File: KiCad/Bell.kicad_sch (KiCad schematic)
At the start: 29 parts, among them J1 USB-C, J2 POWER, J3 Conn_01x10, U1 ESP32-WROOM-32, U2 FT231XQ, U3 ISL89410, U4 ISL89410, U5 LMR16006YQ3, U6 AA, U7 QR

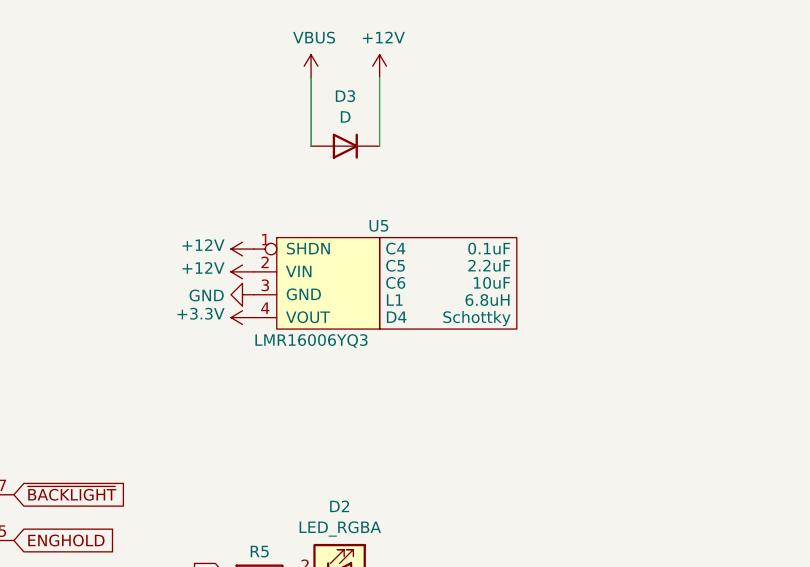
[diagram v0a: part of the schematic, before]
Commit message: More KiCad 6 tweaks
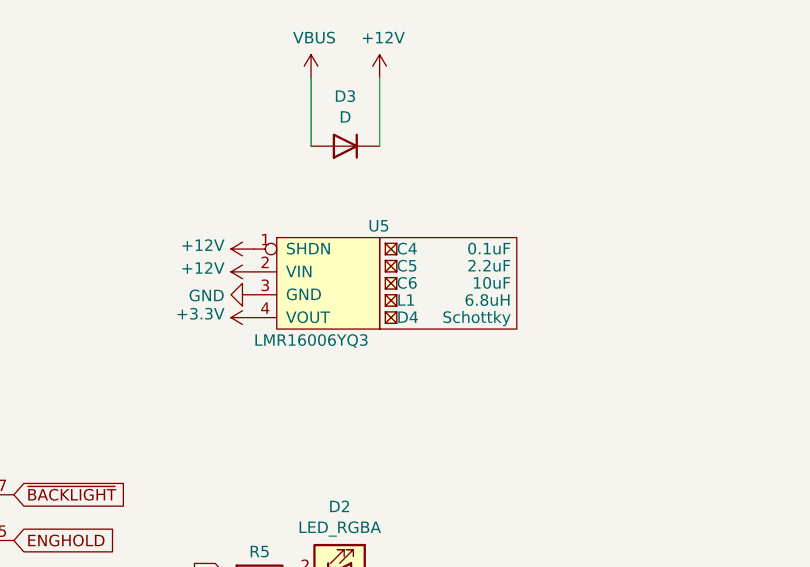
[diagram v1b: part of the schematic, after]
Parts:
- U1: footprint RevK:ESP32-WROOM-32 -> RF_Module:ESP32-WROOM-32
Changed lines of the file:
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@@
   (title_block
     (title "bell box control")
-    (date "2021-07-20")
+    (date "${DATE}")
     (rev "2")
     (company "Adrian Kennard Andrews & Arnold Ltd")
@@
     (property "Reference" "U1" (id 0) (at 53.34 23.3426 0))
     (property "Value" "ESP32-WROOM-32" (id 1) (at 53.34 25.654 0))
-    (property "Footprint" "RevK:ESP32-WROOM-32" (id 2) (at 53.34 101.6 0)
+    (property "Footprint" "RF_Module:ESP32-WROOM-32" (id 2) (at 53.34 101.6 0)
       (effects (font (size 1.27 1.27)) hide)
     )
@@
     (pin "4")
   )
-  (symbol (lib_id "RevK:Hidden") (at 206.375 58.42 0) (unit 1)
-    (in_bom yes) (on_board yes)
-    (property "Reference" "C4" (id 0) (at 205.74 58.42 0)
+  (symbol (lib_name "Hidden_2") (lib_id "RevK:Hidden") (at 206.375 58.42 0) (unit 1)
+    (in_bom yes) (on_board yes)
+    (property "Reference" "C4" (id 0) (at 207.01 58.42 0)
       (effects (font (size 1.27 1.27)) (justify left))
     )
@@
       (effects (font (size 1.27 1.27)) hide)
     )
+    (property "Part No" "" (id 5) (at 206.375 58.42 0)
+      (effects (font (size 1.27 1.27)) hide)
+    )
     (pin "~")
   )
-  (symbol (lib_id "RevK:Hidden") (at 206.375 60.325 0) (unit 1)
-    (in_bom yes) (on_board yes)
-    (property "Reference" "C5" (id 0) (at 205.74 60.325 0)
+  (symbol (lib_name "Hidden_4") (lib_id "RevK:Hidden") (at 206.375 60.325 0) (unit 1)
+    (in_bom yes) (on_board yes)
+    (property "Reference" "C5" (id 0) (at 207.01 60.325 0)
       (effects (font (size 1.27 1.27)) (justify left))
     )
@@
       (effects (font (size 1.27 1.27)) hide)
     )
+    (property "Part No" "" (id 5) (at 206.375 60.325 0)
+      (effects (font (size 1.27 1.27)) hide)
+    )
     (pin "~")
   )
-  (symbol (lib_id "RevK:Hidden") (at 206.375 62.23 0) (unit 1)
-    (in_bom yes) (on_board yes)
-    (property "Reference" "C6" (id 0) (at 205.74 62.23 0)
+  (symbol (lib_name "Hidden_3") (lib_id "RevK:Hidden") (at 206.375 62.23 0) (unit 1)
+    (in_bom yes) (on_board yes)
+    (property "Reference" "C6" (id 0) (at 207.01 62.23 0)
       (effects (font (size 1.27 1.27)) (justify left))
     )
@@
       (effects (font (size 1.27 1.27)) hide)
     )
+    (property "Part No" "" (id 5) (at 206.375 62.23 0)
+      (effects (font (size 1.27 1.27)) hide)
+    )
     (pin "~")
   )
-  (symbol (lib_id "RevK:Hidden") (at 206.375 64.135 0) (unit 1)
-    (in_bom yes) (on_board yes)
-    (property "Reference" "L1" (id 0) (at 205.74 64.135 0)
+  (symbol (lib_name "Hidden_1") (lib_id "RevK:Hidden") (at 206.375 64.135 0) (unit 1)
+    (in_bom yes) (on_board yes)
+    (property "Reference" "L1" (id 0) (at 207.01 64.135 0)
       (effects (font (size 1.27 1.27)) (justify left))
     )
@@
       (effects (font (size 1.27 1.27)) hide)
     )
+    (property "Note" "" (id 6) (at 206.375 64.135 0)
+      (effects (font (size 1.27 1.27)) hide)
+    )
     (pin "~")
   )
   (symbol (lib_id "RevK:Hidden") (at 206.375 66.04 0) (unit 1)
     (in_bom yes) (on_board yes)
-    (property "Reference" "D4" (id 0) (at 205.74 66.04 0)
+    (property "Reference" "D4" (id 0) (at 207.01 66.04 0)
       (effects (font (size 1.27 1.27)) (justify left))
     )
@@
     )
     (property "Part No" "CD1206-B2100" (id 5) (at 206.375 66.04 0)
+      (effects (font (size 1.27 1.27)) hide)
+    )
+    (property "Note" "" (id 6) (at 206.375 66.04 0)
       (effects (font (size 1.27 1.27)) hide)
     )
@@
     )
     (path "/00000000-0000-0000-0000-00006043326c"
-      (reference "U1") (unit 1) (value "ESP32-WROOM-32") (footprint "RevK:ESP32-WROOM-32")
+      (reference "U1") (unit 1) (value "ESP32-WROOM-32") (footprint "RF_Module:ESP32-WROOM-32")
     )
     (path "/00000000-0000-0000-0000-00006084108b"

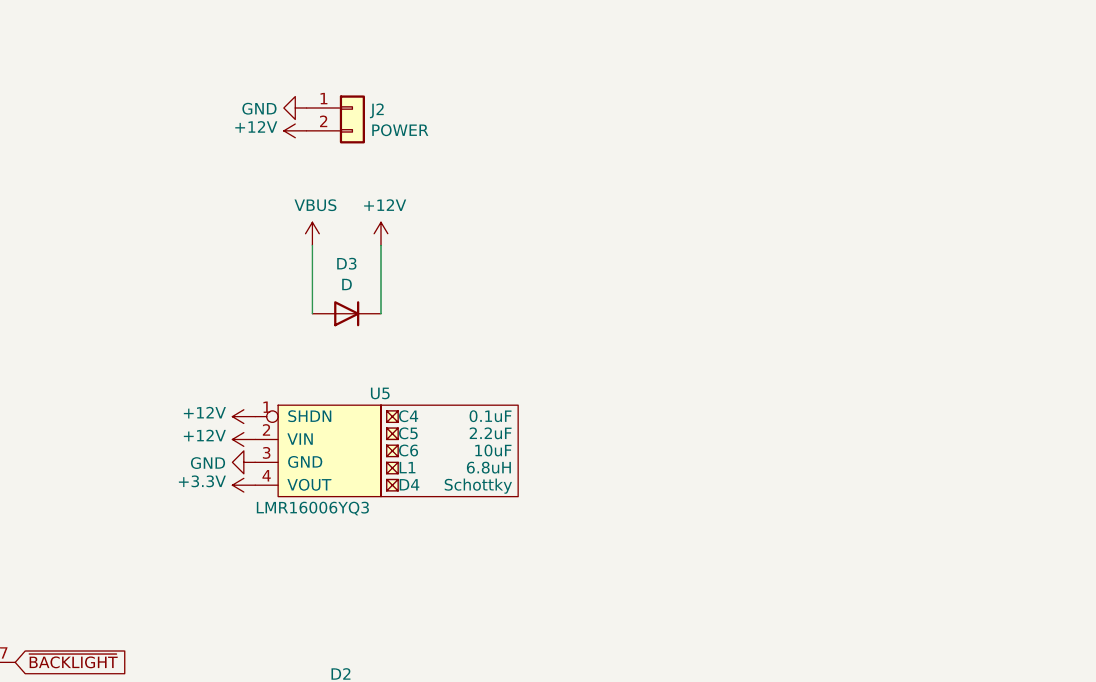
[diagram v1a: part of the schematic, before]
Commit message: New PSU
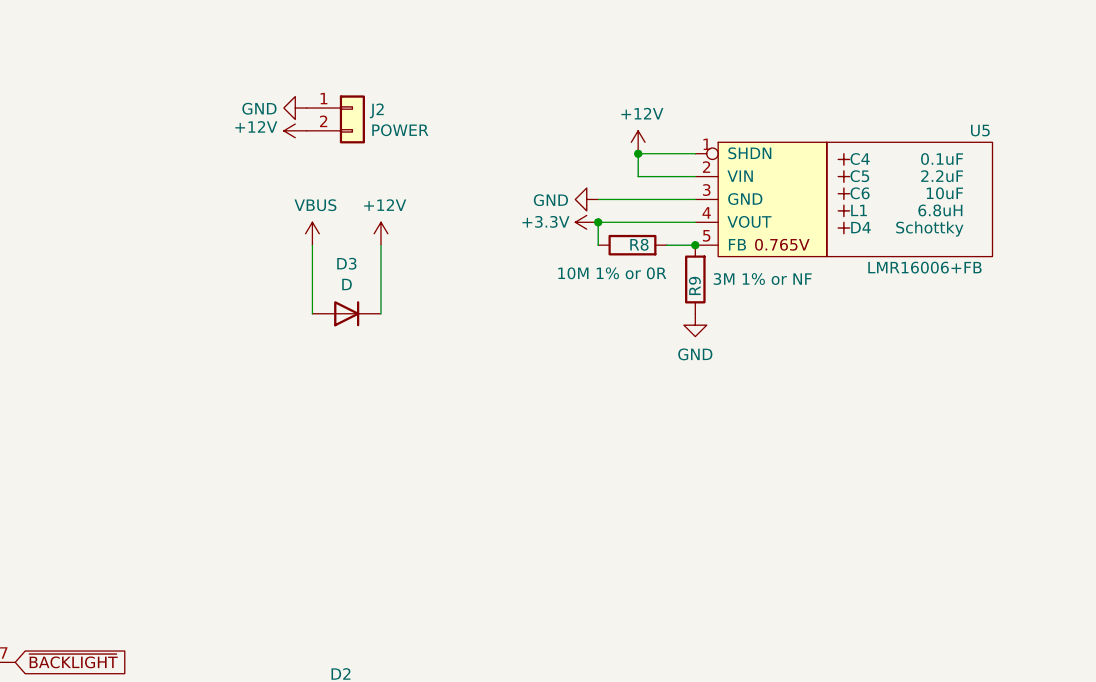
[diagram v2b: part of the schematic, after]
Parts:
- removed U5: LMR16006YQ3, RevK:RegulatorBlock, symbol RevK:LMR16006YQ3
- added R8: 10M 1% or 0R, RevK:R_0603, symbol Device:R
- added R9: 3M 1% or NF, RevK:R_0603, symbol Device:R
- added U5: LMR16006+FB, RevK:RegulatorBlockFB, symbol RevK:LMR16006+FB
- U1: footprint RF_Module:ESP32-WROOM-32 -> RevK:ESP32-WROOM-32
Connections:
- net +12V: now also U5.1 (SHDN), U5.2 (VIN)
- net +3V3: now also R8.1, U5.4 (VOUT)
- net GND: now also R9.1, U5.3 (GND)
- new net: R8.2, R9.2, U5.5 (FB)

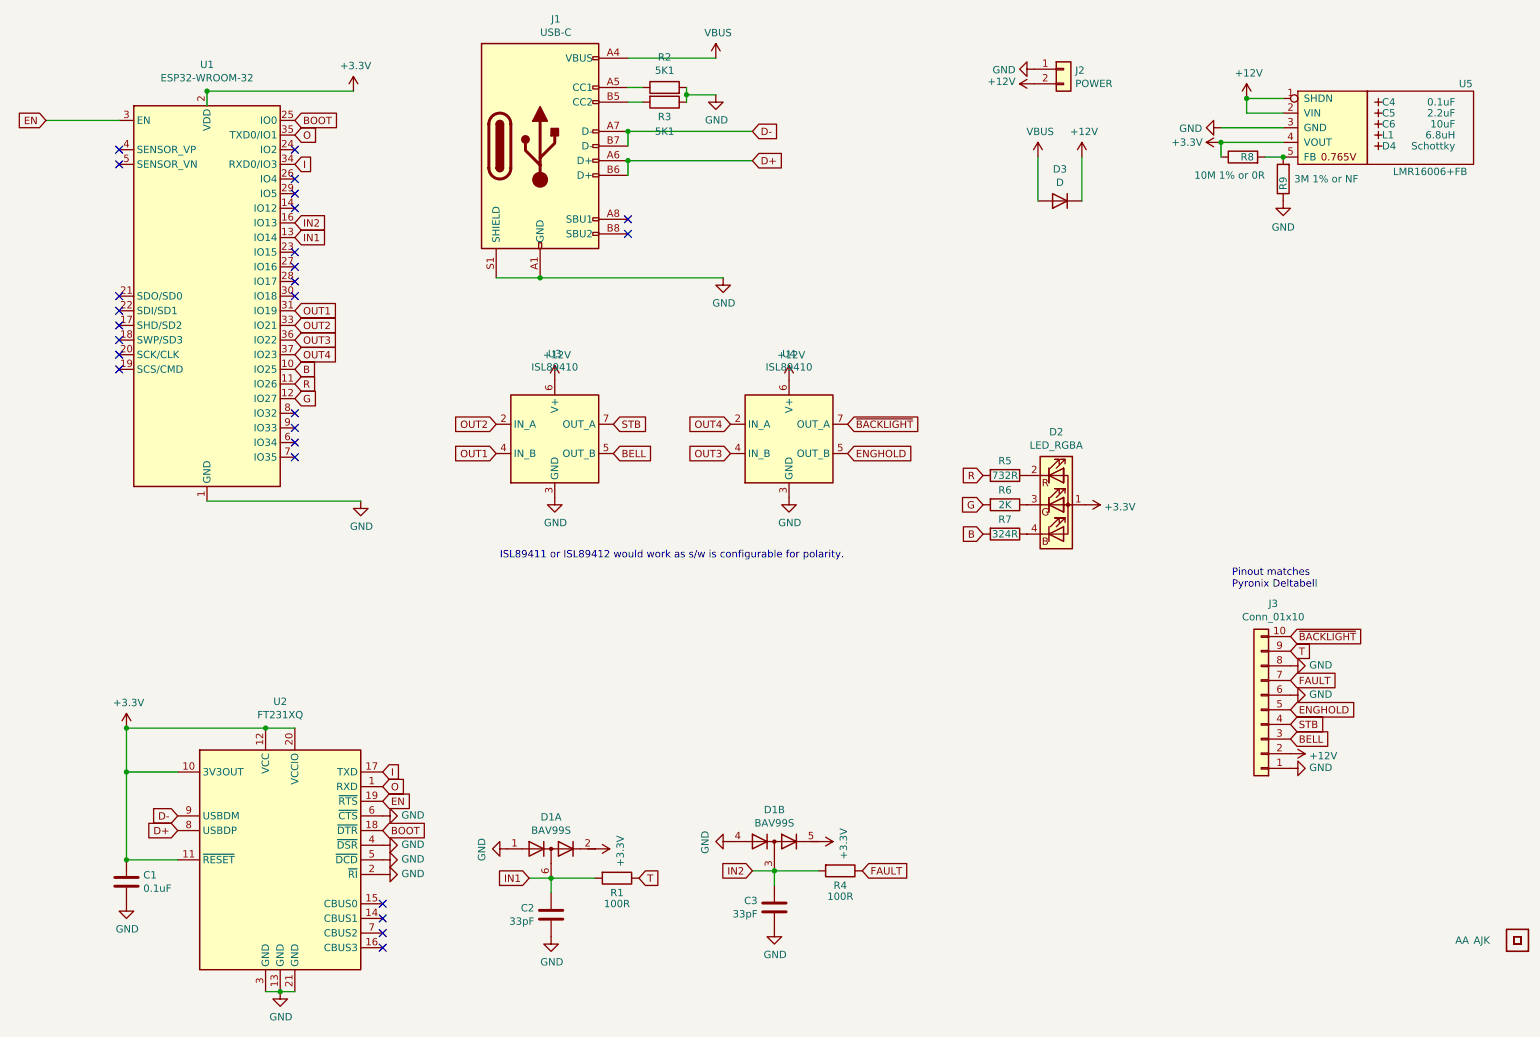
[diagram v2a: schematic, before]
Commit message: VBUS update
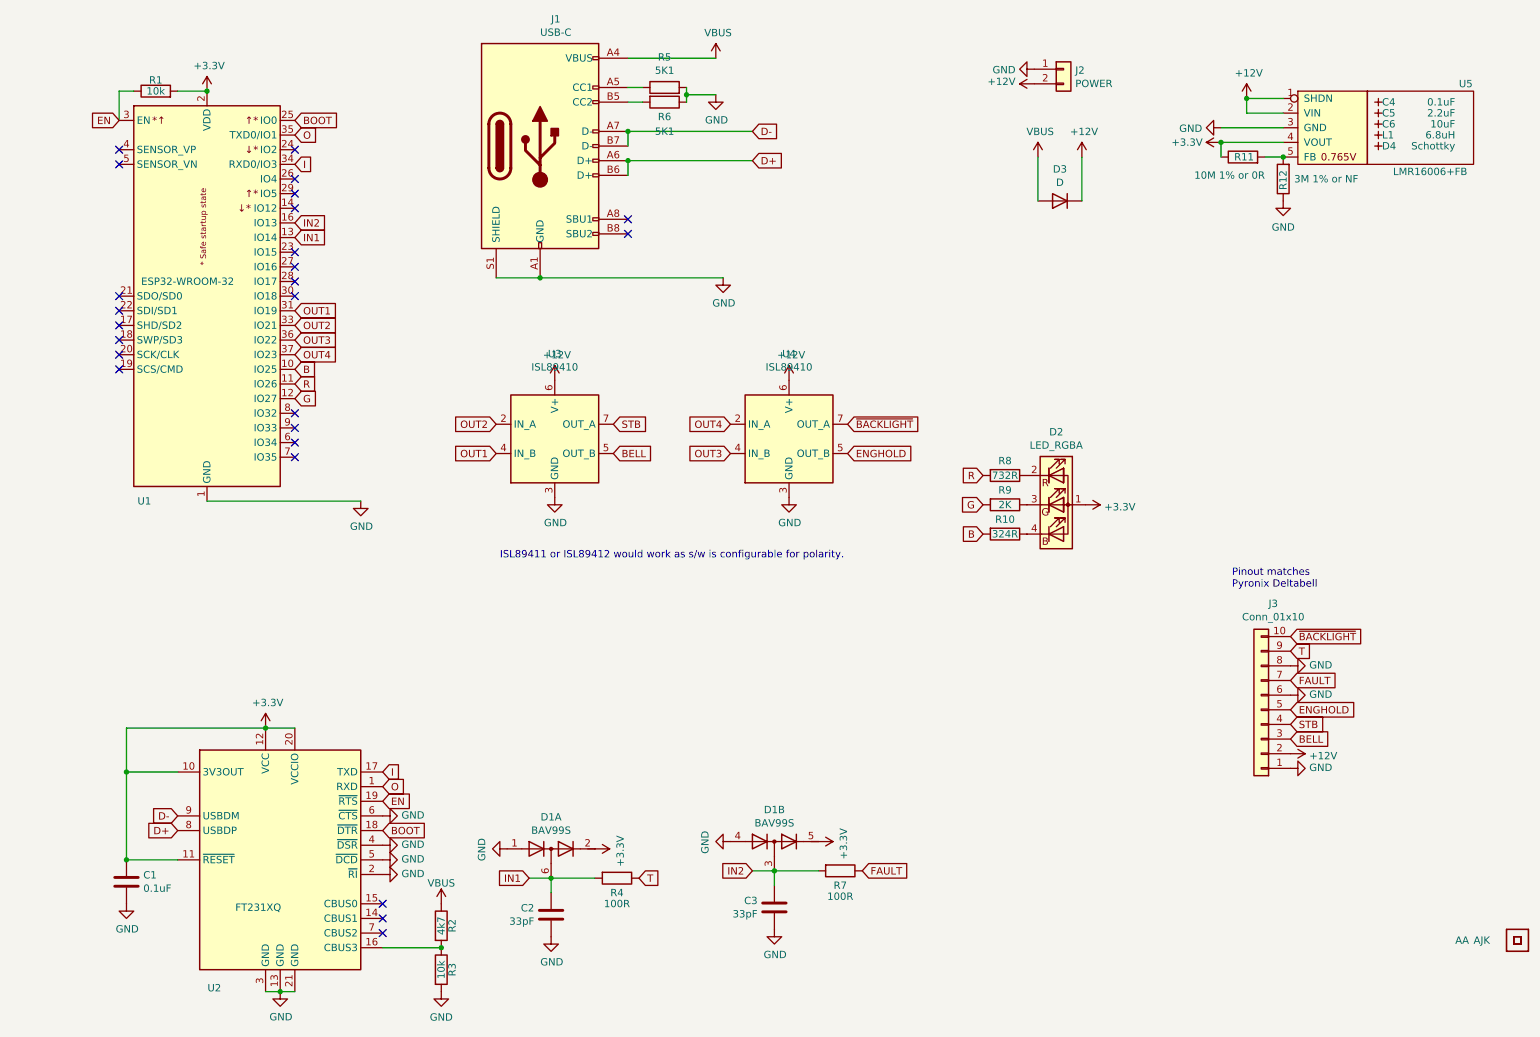
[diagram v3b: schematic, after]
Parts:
- removed U1: ESP32-WROOM-32, RevK:ESP32-WROOM-32, symbol RF_Module:ESP32-WROOM-32
- added R1, R3: 10k, RevK:R_0603, symbol Device:R
- added R2: 4k7, RevK:R_0603, symbol Device:R
- added U1: ESP32-WROOM-32, RevK:ESP32-WROOM-32, symbol RevK:ESP32-WROOM-32
- renumbered R7 to R10, R8 to R11, R9 to R12, R1 to R4, R2 to R5, R3 to R6, R4 to R7, R5 to R8, R6 to R9
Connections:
- net +3V3: now also R1.2, U1.2 (VDD)
- net B: now also U1.10 (IO25)
- net BOOT: now also U1.25 (IO0)
- net EN: now also R1.1, U1.3 (EN)
- net G: now also U1.12 (IO27)
- net GND: now also R3.2, U1.1 (GND), U1.15 (GND), U1.38 (GND), U1.39 (GND)
- net I: now also U1.34 (RXD0/IO3)
- net IN1: now also U1.13 (IO14)
- net IN2: now also U1.16 (IO13)
- net O: now also U1.35 (TXD0/IO1)
- net OUT1: now also U1.31 (IO19)
- net OUT2: now also U1.33 (IO21)
- net OUT3: now also U1.36 (IO22)
- net OUT4: now also U1.37 (IO23)
- net R: now also U1.11 (IO26)
- net VBUS: now also R2.1
- net at U2.16 (CBUS3): now also R2.2, R3.1
- no-connect marks 26 -> 25
